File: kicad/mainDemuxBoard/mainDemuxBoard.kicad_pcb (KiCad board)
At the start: 4 copper layers, 150.2 x 150 mm, 221 parts, among them J1 Conn_02x20_Top_Bottom, J10 Conn_02x20_Top_Bottom, J11 Conn_02x20_Top_Bottom, J12 Conn_02x20_Top_Bottom, J13 Conn_02x20_Top_Bottom, J14 Conn_02x20_Top_Bottom, J15 Conn_02x20_Top_Bottom, J16 Conn_02x20_Top_Bottom, J17 Conn_02x20_Top_Bottom, J2 Conn_02x20_Top_Bottom, J3 Conn_02x20_Top_Bottom, J4 Conn_02x20_Top_Bottom, J5 Conn_02x20_Top_Bottom, J6 Conn_02x20_Top_Bottom, J7 Conn_02x20_Top_Bottom, J8 Conn_02x20_Top_Bottom, J9 Conn_02x20_Top_Bottom, Q1 Q_PMOS_GSD, Q10 Q_PMOS_GSD, Q100 Q_PMOS_GSD, Q101 Q_PMOS_GSD, Q102 Q_PMOS_GSD, Q103 Q_PMOS_GSD, Q104 Q_NMOS_GSD, Q105 Q_NMOS_GSD, Q106 Q_NMOS_GSD, Q107 Q_NMOS_GSD, Q108 Q_NMOS_GSD, Q109 Q_PMOS_GSD, Q11 Q_PMOS_GSD, Q110 Q_PMOS_GSD, Q111 Q_PMOS_GSD, Q112 Q_PMOS_GSD, Q113 Q_PMOS_GSD, Q114 Q_NMOS_GSD, Q115 Q_NMOS_GSD, Q116 Q_NMOS_GSD, Q117 Q_NMOS_GSD, Q118 Q_NMOS_GSD, Q119 Q_PMOS_GSD, Q12 Q_PMOS_GSD, Q120 Q_PMOS_GSD, Q121 Q_PMOS_GSD, Q122 Q_PMOS_GSD, Q123 Q_PMOS_GSD, Q124 Q_NMOS_GSD, Q125 Q_NMOS_GSD, Q126 Q_NMOS_GSD, Q127 Q_NMOS_GSD, Q128 Q_NMOS_GSD, Q129 Q_PMOS_GSD, Q13 Q_PMOS_GSD, Q130 Q_PMOS_GSD, Q131 Q_PMOS_GSD, Q132 Q_PMOS_GSD, Q133 Q_PMOS_GSD, Q134 Q_NMOS_GSD, Q135 Q_NMOS_GSD, Q136 Q_NMOS_GSD, Q137 Q_NMOS_GSD, Q138 Q_NMOS_GSD, Q139 Q_PMOS_GSD, Q14 Q_NMOS_GSD, Q140 Q_PMOS_GSD, Q141 Q_PMOS_GSD, Q142 Q_PMOS_GSD, Q143 Q_PMOS_GSD, Q144 Q_NMOS_GSD, Q145 Q_NMOS_GSD, Q146 Q_NMOS_GSD, Q147 Q_NMOS_GSD, Q148 Q_NMOS_GSD, Q149 Q_NMOS_GSD, Q15 Q_NMOS_GSD, Q150 Q_NMOS_GSD, Q151 Q_PMOS_GSD, Q152 Q_PMOS_GSD, Q153 Q_NMOS_GSD, Q154 Q_NMOS_GSD, Q155 Q_PMOS_GSD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

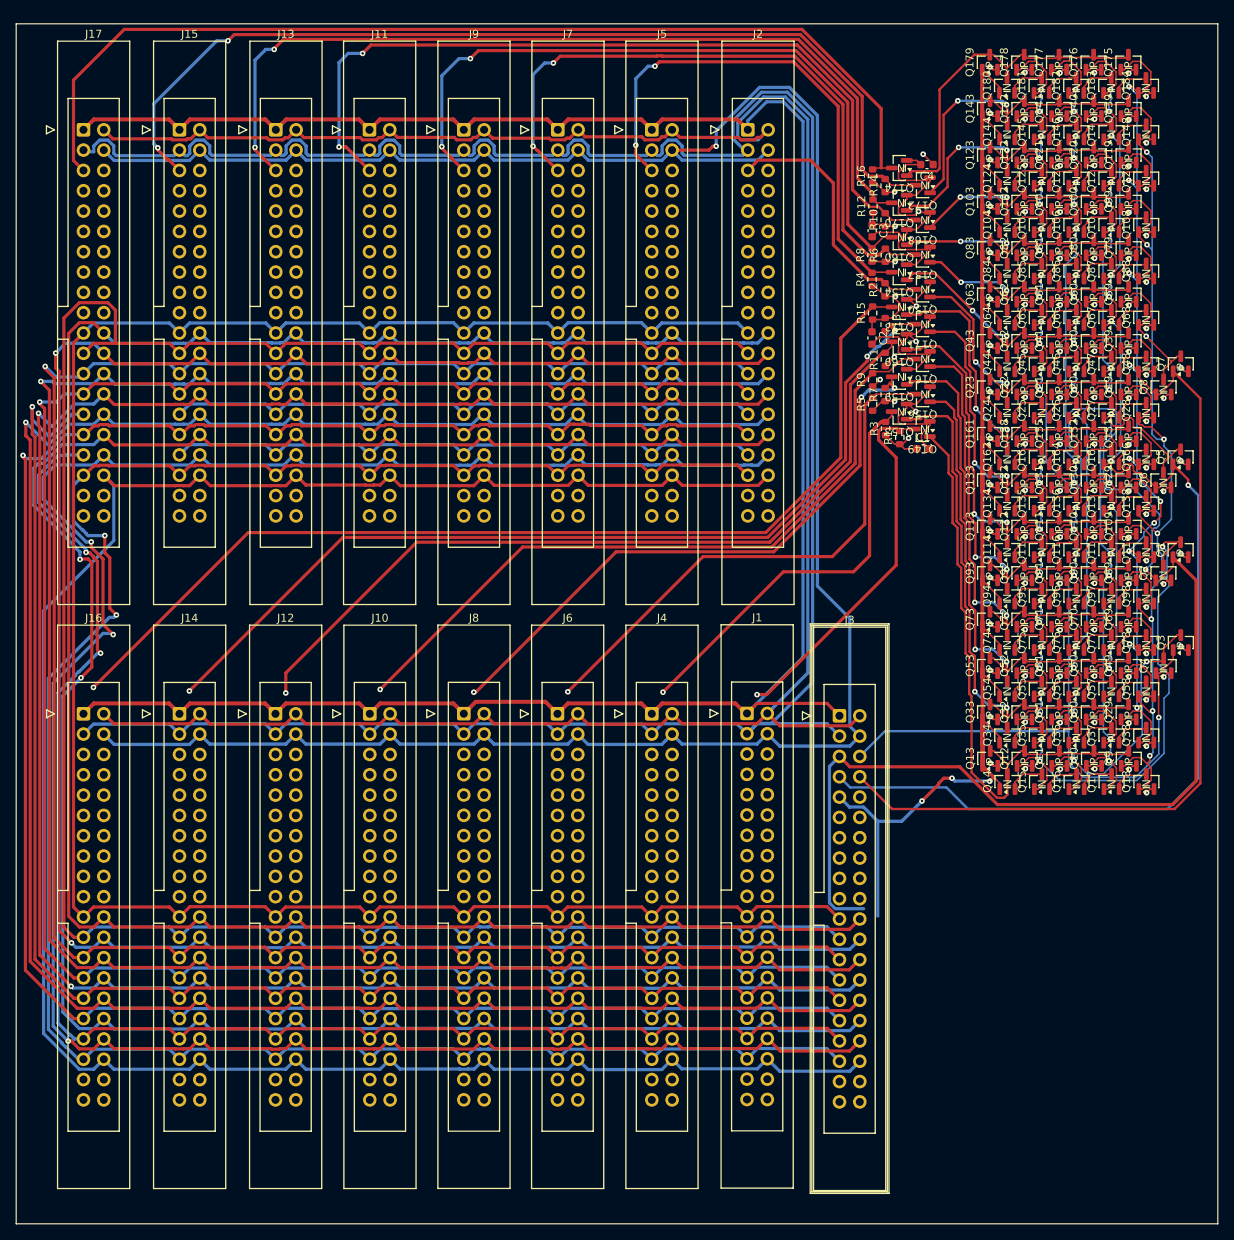
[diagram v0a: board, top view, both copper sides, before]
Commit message: update bom, add more capacitors
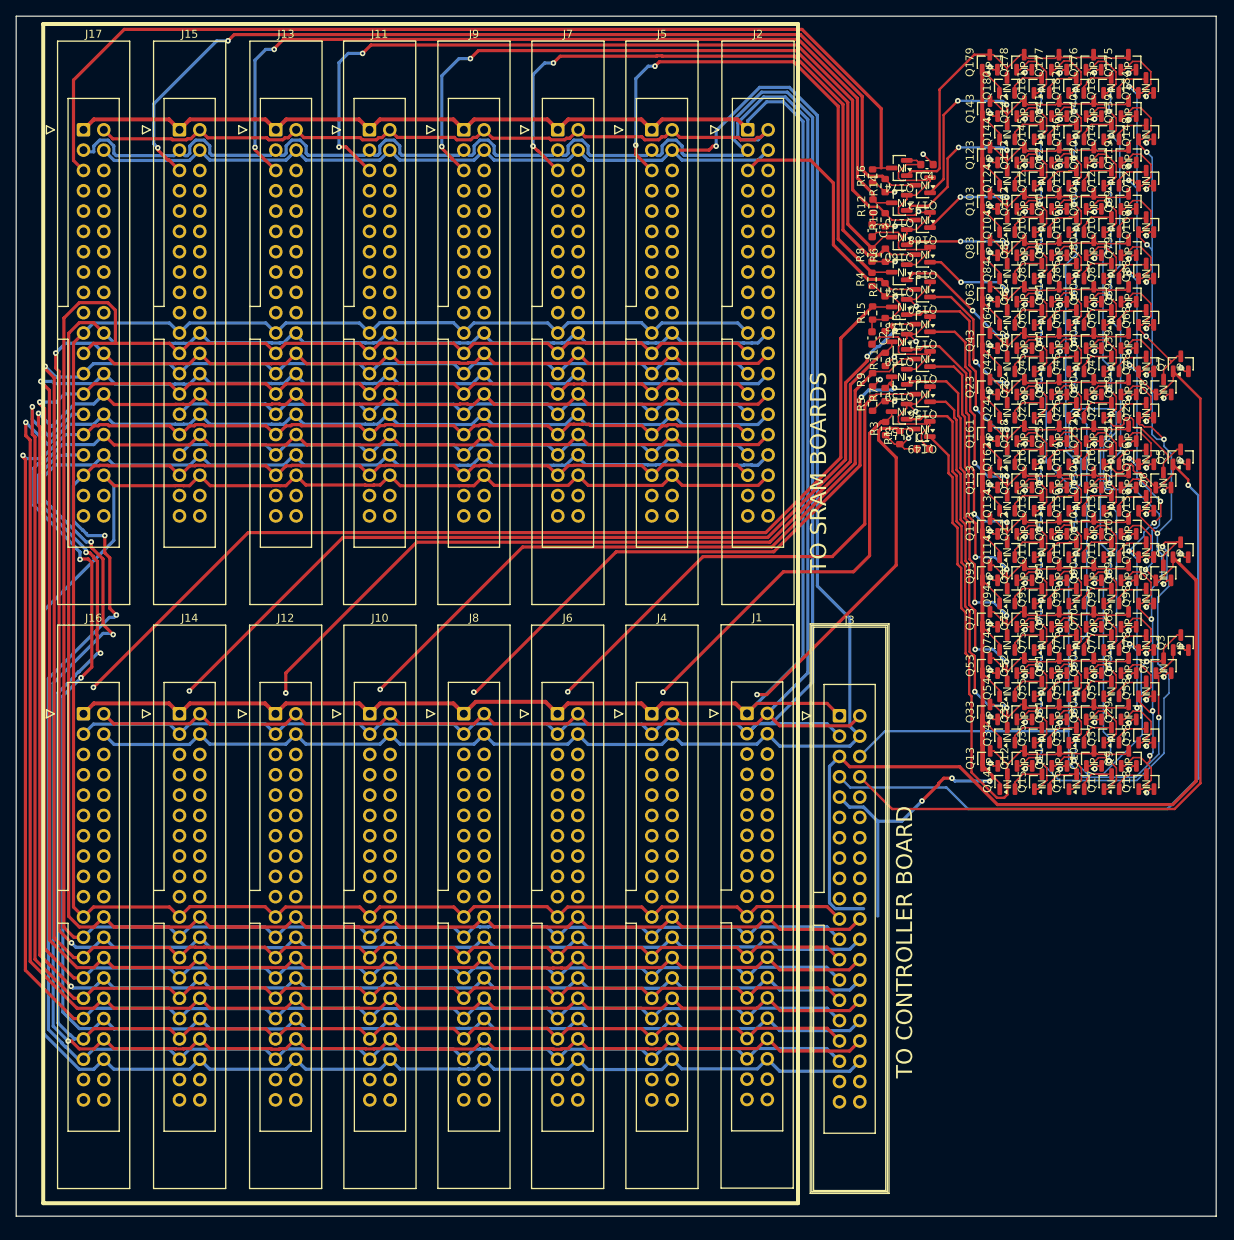
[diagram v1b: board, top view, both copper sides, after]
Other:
- board size 150.2 x 150 mm -> 150 x 150 mm
- board text added: "TO CONTROLLER BOARD"
- board text added: "TO SRAM BOARDS"
